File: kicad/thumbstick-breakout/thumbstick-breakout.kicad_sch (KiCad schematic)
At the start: 4 parts, among them J1 59453-051110ECHLF

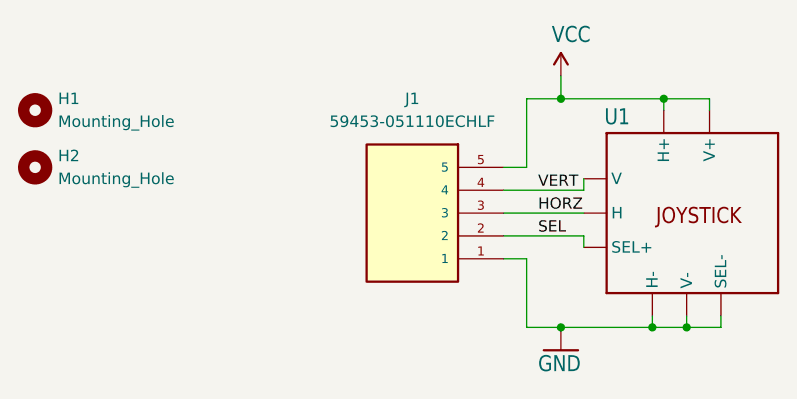
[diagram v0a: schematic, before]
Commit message: Add joystick breakout
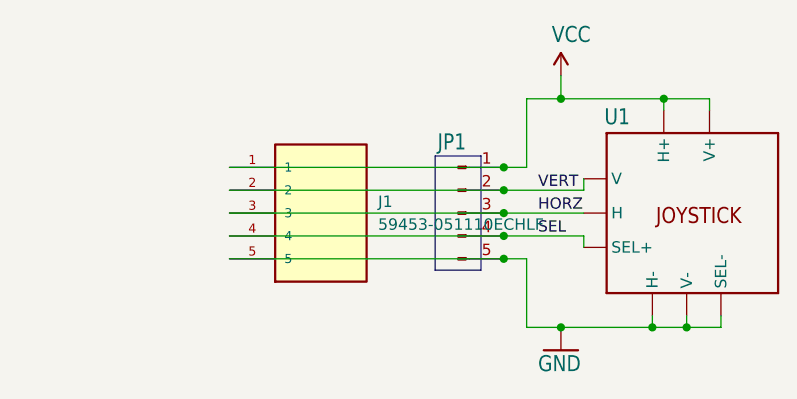
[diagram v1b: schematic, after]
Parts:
- removed H1, H2: Mounting_Hole, MountingHole:MountingHole_2.2mm_M2_Pad_Via, symbol ScottoKeebs:Placeholder_Mounting_Hole
- added JP1: ~, thumbstick-breakout:1x05, symbol Connector:Conn_01x05_Pin
- U1: footprint footprints:Joystick -> thumbstick-breakout:Joystick; symbol thumbstick:Joystick -> thumbstick-breakout:Joystick
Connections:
- net GND: now also J1.5, JP1.5 (Pin_5); no longer J1.1
- net HORZ: now also JP1.3 (Pin_3)
- net SEL: now also J1.4, JP1.4 (Pin_4); no longer J1.2
- net VCC: now also J1.1, JP1.1 (Pin_1); no longer J1.5
- net VERT: now also J1.2, JP1.2 (Pin_2); no longer J1.4

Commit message: Use only fcc on thumbstick
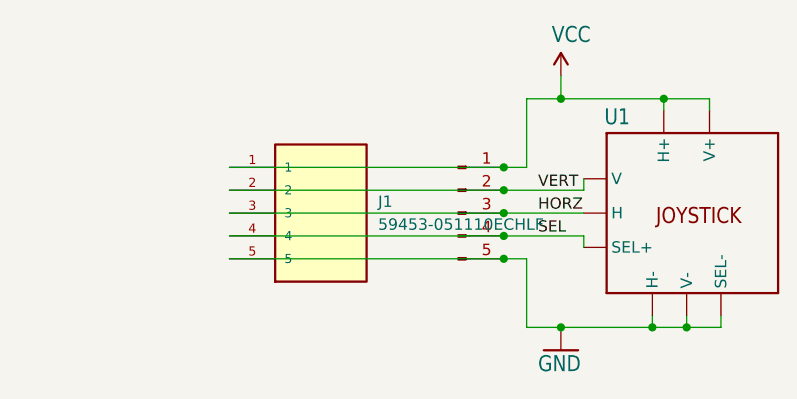
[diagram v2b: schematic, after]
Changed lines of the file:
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@@
-		)
-	)
-	(rectangle
-		(start 128.27 90.17)
-		(end 133.35 102.87)
-		(stroke
-			(width 0)
-			(type default)
-			(color 0 0 0 1)
-		)
-		(fill
-			(type none)
 		)
 	)
@@
 				)
 				(justify left bottom)
+				(hide yes)
 			)
 		)
